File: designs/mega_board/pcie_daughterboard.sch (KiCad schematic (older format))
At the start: 13 parts

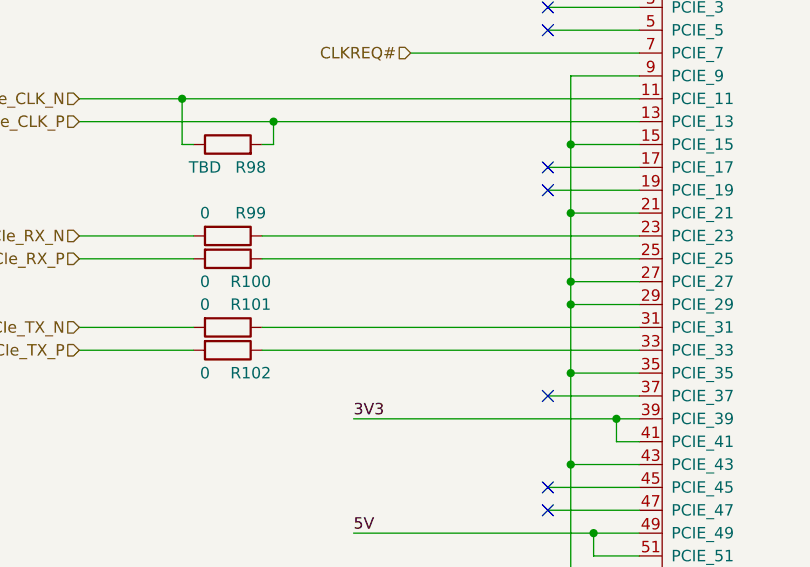
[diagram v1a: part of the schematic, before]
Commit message: Add label to differential pair for routing
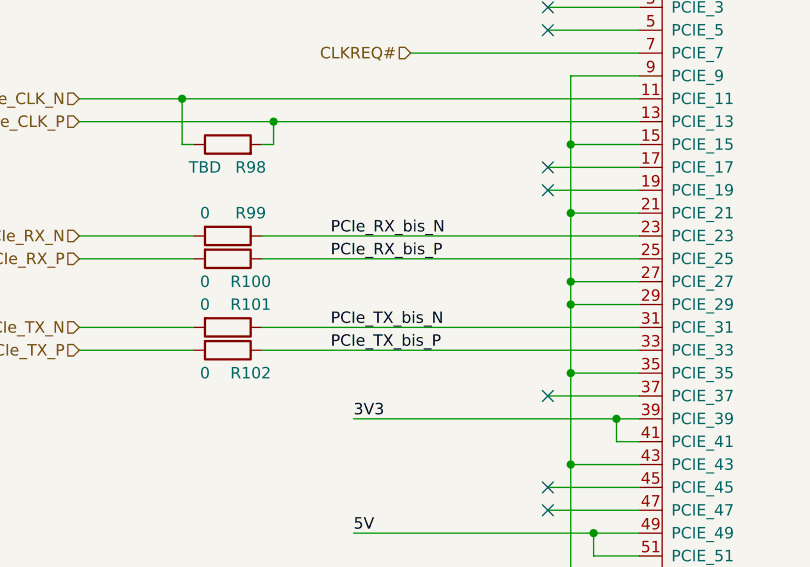
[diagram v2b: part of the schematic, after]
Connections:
- net PCIe_RX_bis_N: now reaches PCIE0.23 (PCIE_23), R99.1
- net PCIe_RX_bis_P: now reaches PCIE0.25 (PCIE_25), R100.1
- net PCIe_TX_bis_N: now reaches PCIE0.31 (PCIE_31), R101.1
- net PCIe_TX_bis_P: now reaches PCIE0.33 (PCIE_33), R102.1
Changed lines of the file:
@@
 AR Path="/5D032C97/5D19F8AF" Ref="#PWR0173"  Part="1"
 AR Path="/5D1650F5/5D19F8AF" Ref="#PWR0190"  Part="1"
-F 0 "#PWR0190" H 6650 5600 50  0001 C CNN
+F 0 "#PWR0173" H 6650 5600 50  0001 C CNN
 F 1 "GND" H 6655 5677 50  0000 C CNN
 F 2 "" H 6650 5850 50  0001 C CNN
@@
 AR Path="/5D032C97/5D1C58DE" Ref="#PWR0174"  Part="1"
 AR Path="/5D1650F5/5D1C58DE" Ref="#PWR0191"  Part="1"
-F 0 "#PWR0191" H 2800 1850 50  0001 C CNN
+F 0 "#PWR0174" H 2800 1850 50  0001 C CNN
 F 1 "GND" H 2805 1927 50  0000 C CNN
 F 2 "" H 2800 2100 50  0001 C CNN
@@
 AR Path="/5D032C97/5D1D537C" Ref="#PWR0175"  Part="1"
 AR Path="/5D1650F5/5D1D537C" Ref="#PWR0192"  Part="1"
-F 0 "#PWR0192" H 1700 1850 50  0001 C CNN
+F 0 "#PWR0175" H 1700 1850 50  0001 C CNN
 F 1 "GND" H 1705 1927 50  0000 C CNN
 F 2 "" H 1700 2100 50  0001 C CNN
@@
 AR Path="/5D032C97/5D20ABC1" Ref="#PWR0176"  Part="1"
 AR Path="/5D1650F5/5D20ABC1" Ref="#PWR0193"  Part="1"
-F 0 "#PWR0193" H 4650 5600 50  0001 C CNN
+F 0 "#PWR0176" H 4650 5600 50  0001 C CNN
 F 1 "GND" H 4655 5677 50  0000 C CNN
 F 2 "" H 4650 5850 50  0001 C CNN
@@
 Wire Wire Line
 	4550 4800 4950 4800
+Text Label 3600 4100 0    50   ~ 0
+PCIe_RX_bis_N
+Text Label 3600 4200 0    50   ~ 0
+PCIe_RX_bis_P
+Text Label 3600 4500 0    50   ~ 0
+PCIe_TX_bis_N
+Text Label 3600 4600 0    50   ~ 0
+PCIe_TX_bis_P
 $EndSCHEMATC
